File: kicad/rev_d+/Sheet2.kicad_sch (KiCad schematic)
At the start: 227 parts, among them J10 vg_old, J12 JUMPER, J13 JUMPER, J14 JUMPER, J5 JUMPER, J6 JUMPER, J8 JUMPER, J9 JUMPER, Q2 QUARTZ, Q3 QUARTZ32768, X11 KEYB-MOUSE, X12 IDC20, X13 USB_C, X15 PLB2-2, X19 WCH LinkE pgm conn, X21 Turbosound conn, X22 PS2 extra input, X23 SEGA pads, X25 USB_C device, X27 USB_A, X28 RJ45_Hanrun_HR911105A_Horizon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, X29 RS232_9, X3 IDC26LPT, X4 IDC10M, X5 IDC10M, X6 IDC10M

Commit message: pentevo: rev D+: change level shifter for PS/2 to NMOS-based (save 4 pins), connect forgotten nCONFIG/nSTATUS/CONFDONE pins
git-svn-id: svn://localhost/local-pentevo@1313 c6c76956-fad2-4150-a3a9-ea0a427205ba
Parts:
- removed C55, C62: 0.1uF, C-CHIP, symbol eva-altium-import:Sheet2_3_mirrored_CAPCHIP
- removed D15, D22: 74HCT125, symbol 74xx:74LS125
- removed R123, R124, R125, R126: 10K, R-CHIP, symbol eva-altium-import:Sheet2_3_mirrored_RESCHIP
- removed R176, R201, R202, R31: 5K1, R-CHIP, symbol eva-altium-import:Sheet2_0_RESCHIP
- added DA16, DA17, DA18: USBLC6-4SC6, Package_TO_SOT_SMD:SOT-23-6, symbol Power_Protection:USBLC6-4SC6
- added R123, R124, R125, R126, R176, R201, R202, R31: 10K, R-CHIP, symbol eva-altium-import:Sheet2_1_RESCHIP
- added VT14, VT15, VT16, VT17: 2N7002, Package_TO_SOT_SMD:SOT-23, symbol Transistor_FET:2N7002
- C56: value 20pF -> 100pF
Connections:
- net PS2_KB_CLK_O is gone; now on net ~{STATUS}: D4.18 (PC3)
- net PS2_KB_DAT_O is gone; now on net ~{CONFIG}: D4.17 (PC2)
- net PS2_MS_DAT_O is gone; now on net CONFDONE: D4.33 (PC4)
- net GND: now also DA16.2 (GND), DA17.5 (VBUS), DA18.5 (VBUS)
- net PS2_KEYB_CLK: now also DA16.3 (I/O2), R124.1 (i/o), VT15.3 (D)
- net PS2_KEYB_DAT: now also DA16.1 (I/O1), R125.1 (i/o), VT14.3 (D)
- net PS2_MOUS_CLK: now also DA16.6 (I/O4), R123.2 (i/o1), VT17.3 (D)
- net PS2_MOUS_DAT: now also DA16.4 (I/O3), R31.2 (i/o1), VT16.3 (D)
- net USBDEV+: now also DA17.1 (I/O1), DA17.6 (I/O4)
- net USBDEV-: now also DA17.3 (I/O2), DA17.4 (I/O3)
- net USBHOST+: now also DA18.1 (I/O1), DA18.6 (I/O4)
- net USBHOST-: now also DA18.3 (I/O2), DA18.4 (I/O3)
- net VCC33_MCU: now also R126.2 (i/o1), R176.2 (i/o1), R201.2 (i/o1), R202.2 (i/o1), VT14.1 (G), VT15.1 (G), VT16.1 (G), VT17.1 (G)
- net VCC5: now also DA16.5 (VBUS), R123.1 (i/o), R124.2 (i/o1), R125.2 (i/o1), R31.1 (i/o)
- net VCC5_MCU: now also DA18.2 (GND)
- net at R200.1 (i/o), X25.A4 (VBUS), X25.A9 (VBUS)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: now also DA17.2 (GND)
- net PS2_KB_CLK_I renamed PS2_KB_CLK_3v3
- net PS2_KB_CLK_3v3: now also R202.1 (i/o), VT15.2 (S)
- net PS2_KB_DAT_I renamed PS2_KB_DAT_3v3
- net PS2_KB_DAT_3v3: now also R201.1 (i/o), VT14.2 (S)
- net PS2_MS_CLK_I renamed PS2_MS_CLK_3v3
- net PS2_MS_CLK_3v3: now also R176.1 (i/o), VT17.2 (S)
- net PS2_MS_CLK_O: no longer names the net of D4.34 (PC5)
- net PS2_MS_DAT_I renamed PS2_MS_DAT_3v3
- net PS2_MS_DAT_3v3: now also R126.1 (i/o), VT16.2 (S)
- no-connect marks 37 -> 38
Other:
- moved on the sheet: C105, C122, C36, C37, C50, C56, C83, D20A, D20B, D20C, D20D, D20E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

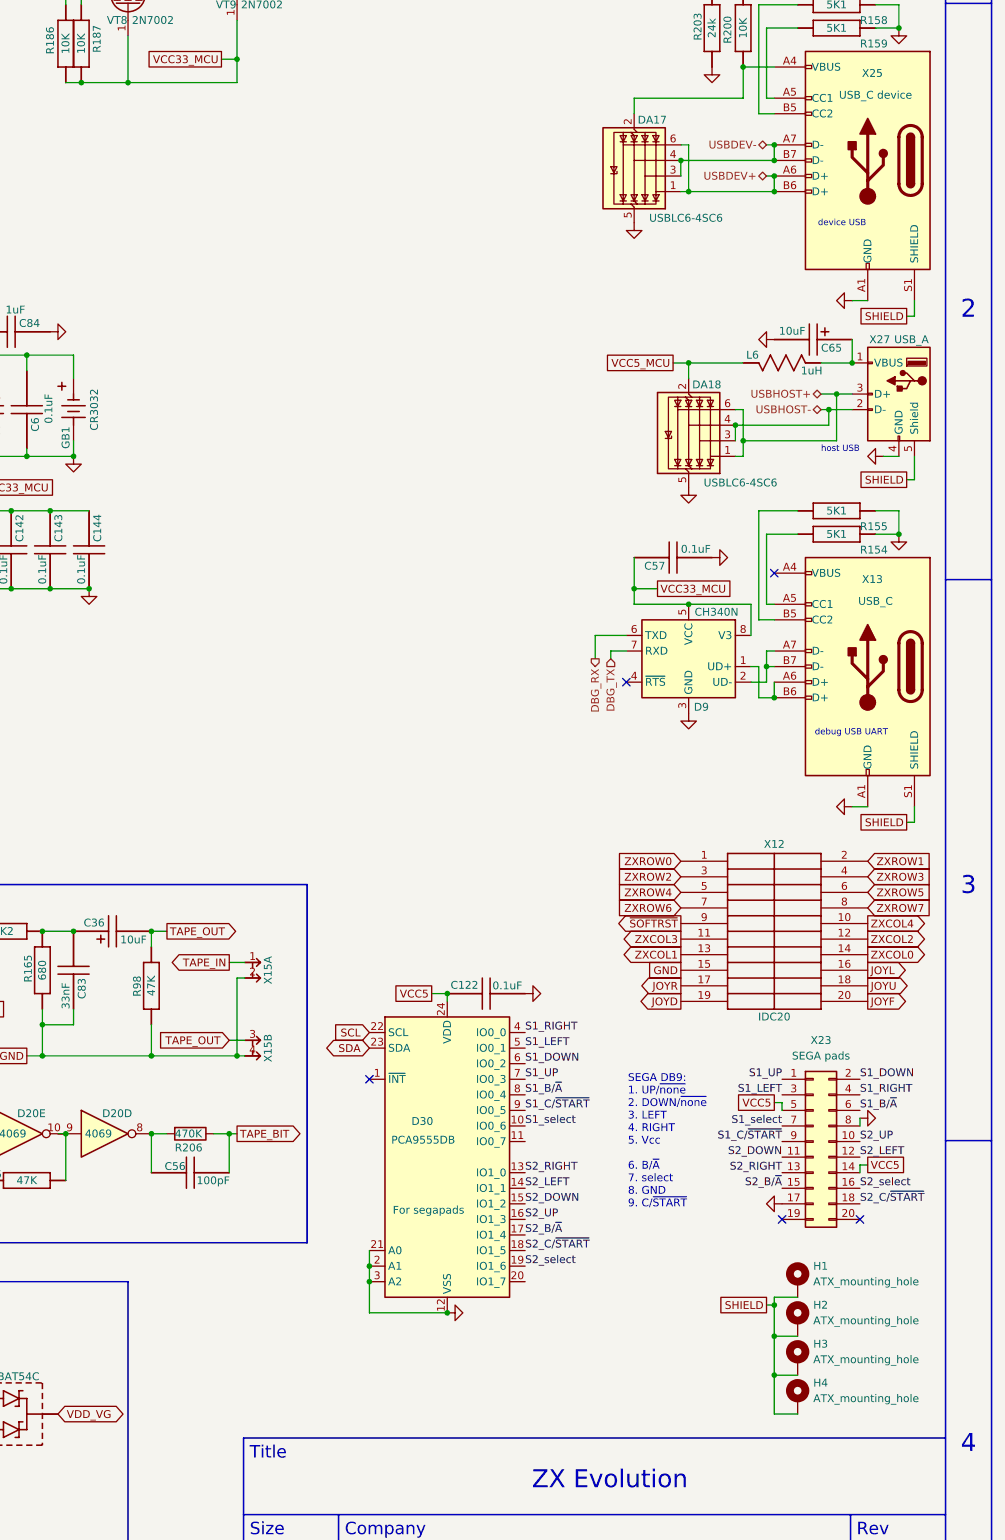
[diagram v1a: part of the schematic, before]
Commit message: pentevo: rev D+: fix USBLC6 wiring, add FE1.1s hub (WIP)
git-svn-id: svn://localhost/local-pentevo@1331 c6c76956-fad2-4150-a3a9-ea0a427205ba
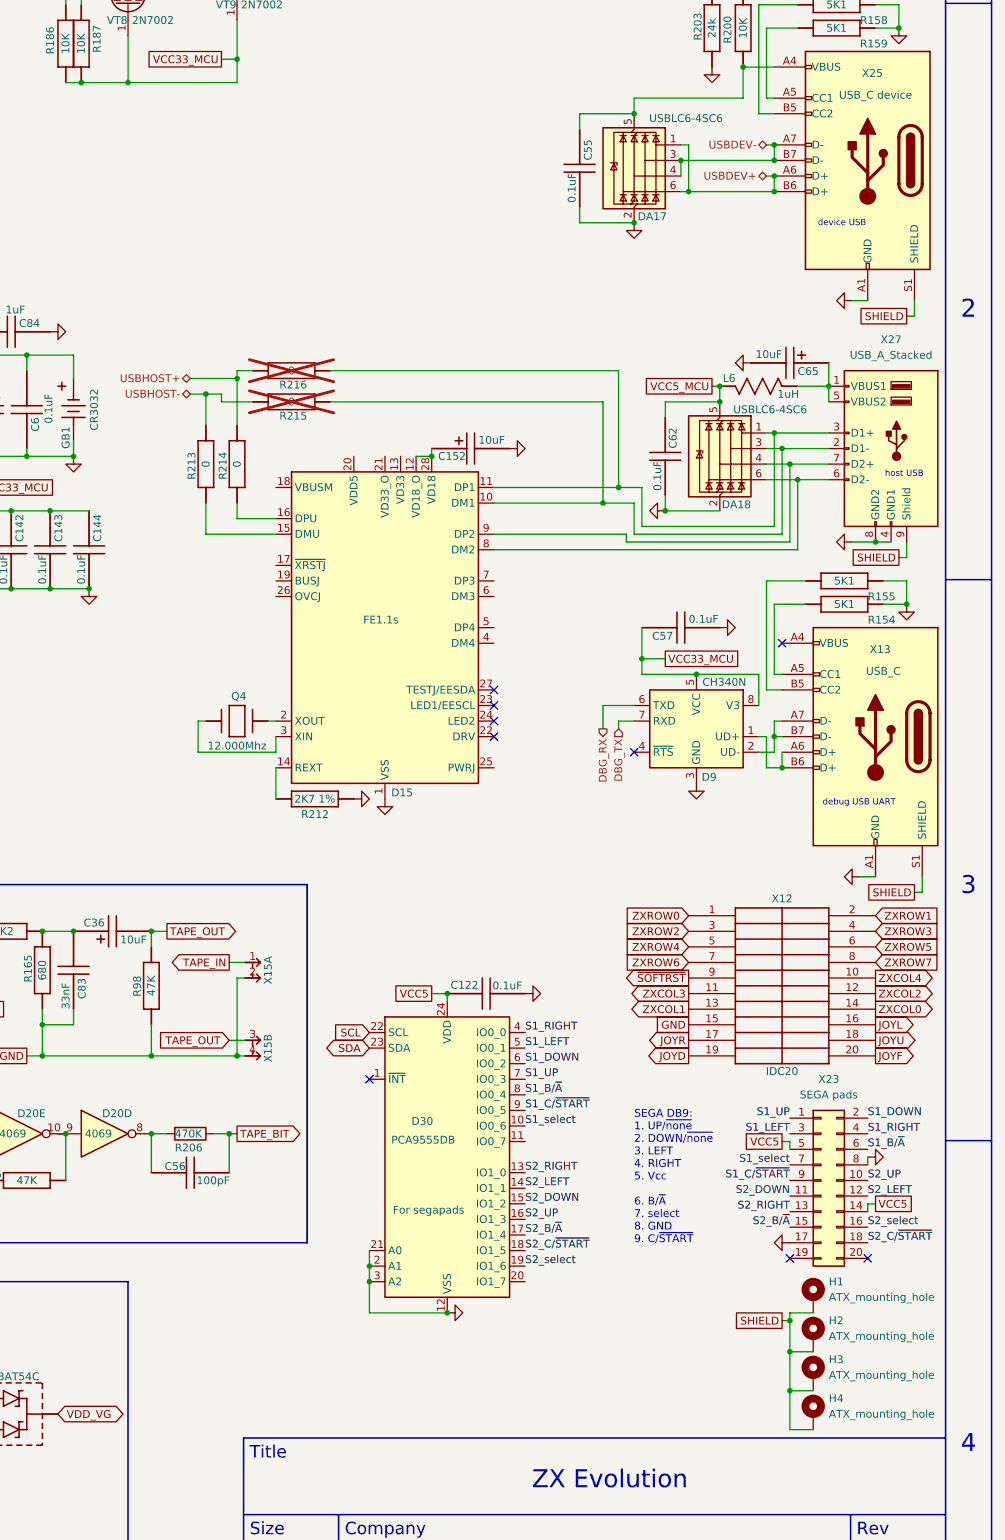
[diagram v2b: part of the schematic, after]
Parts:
- removed X27: USB_A, symbol Connector:USB_A
- added C152: 10uF, EC-CHIP, symbol eva-altium-import:Sheet2_3_ECAPCHIP
- added C55, C62: 0.1uF, C-CHIP, symbol eva-altium-import:Sheet2_2_CAPCHIP
- added D15: FE1.1s, Package_SO:SSOP-28_3.9x9.9mm_P0.635mm, symbol Interface_USB:FE1.1s
- added Q4: QUARTZ, CRYSTAL, symbol eva-altium-import:Sheet2_0_QUARTZ
- added R212: 2K7 1%, R-CHIP, symbol eva-altium-import:Sheet2_0_RESCHIP
- added R213, R214, R215, R216: 0, R-CHIP, symbol eva-altium-import:Sheet1_1_RESCHIP
- added X27: USB_A_Stacked, symbol Connector:USB_A_Stacked
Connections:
- net GND: now also DA17.2 (GND), DA18.2 (GND), C152.2, C55.2, C62.2, D15.1 (VSS), R212.1 (i/o), X27.4 (GND1), X27.8 (GND2); no longer DA17.5 (VBUS), DA18.5 (VBUS)
- net SHIELD: now also X27.9 (Shield)
- net USBHOST+: now also R214.2 (i/o1), R216.2 (i/o1); no longer DA18.1 (I/O1), DA18.6 (I/O4)
- net USBHOST-: now also R213.2 (i/o1), R215.2 (i/o1); no longer DA18.3 (I/O2), DA18.4 (I/O3)
- net VCC5_MCU: now also DA18.5 (VBUS), C62.1; no longer DA18.2 (GND)
- net at R200.1 (i/o), X25.A4 (VBUS), X25.A9 (VBUS)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: now also DA17.5 (VBUS), C55.1; no longer DA17.2 (GND)
- net at C65.1, L6.2: now also X27.1 (VBUS1), X27.5 (VBUS2)
- new net: D15.10 (DM1), DA18.3 (I/O2), R215.1 (i/o), X27.2 (D1-)
- new net: D15.11 (DP1), DA18.1 (I/O1), R216.1 (i/o), X27.3 (D1+)
- new net: D15.8 (DM2), DA18.6 (I/O4), X27.6 (D2-)
- new net: D15.9 (DP2), DA18.4 (I/O3), X27.7 (D2+)
- new net: D15.16 (DPU), R214.1 (i/o)
- new net: D15.14 (REXT), R212.2 (i/o1)
- new net: D15.3 (XIN), Q4.A
- new net: D15.2 (XOUT), Q4.B
- new net: C152.1, D15.12 (VD18_O), D15.28 (VD18)
- new net: D15.15 (DMU), R213.1 (i/o)
- no-connect marks 38 -> 42
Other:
- moved on the sheet: C57, C65, D9, H1, H2, H3, H4, L6, R154, R155, X12, X13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

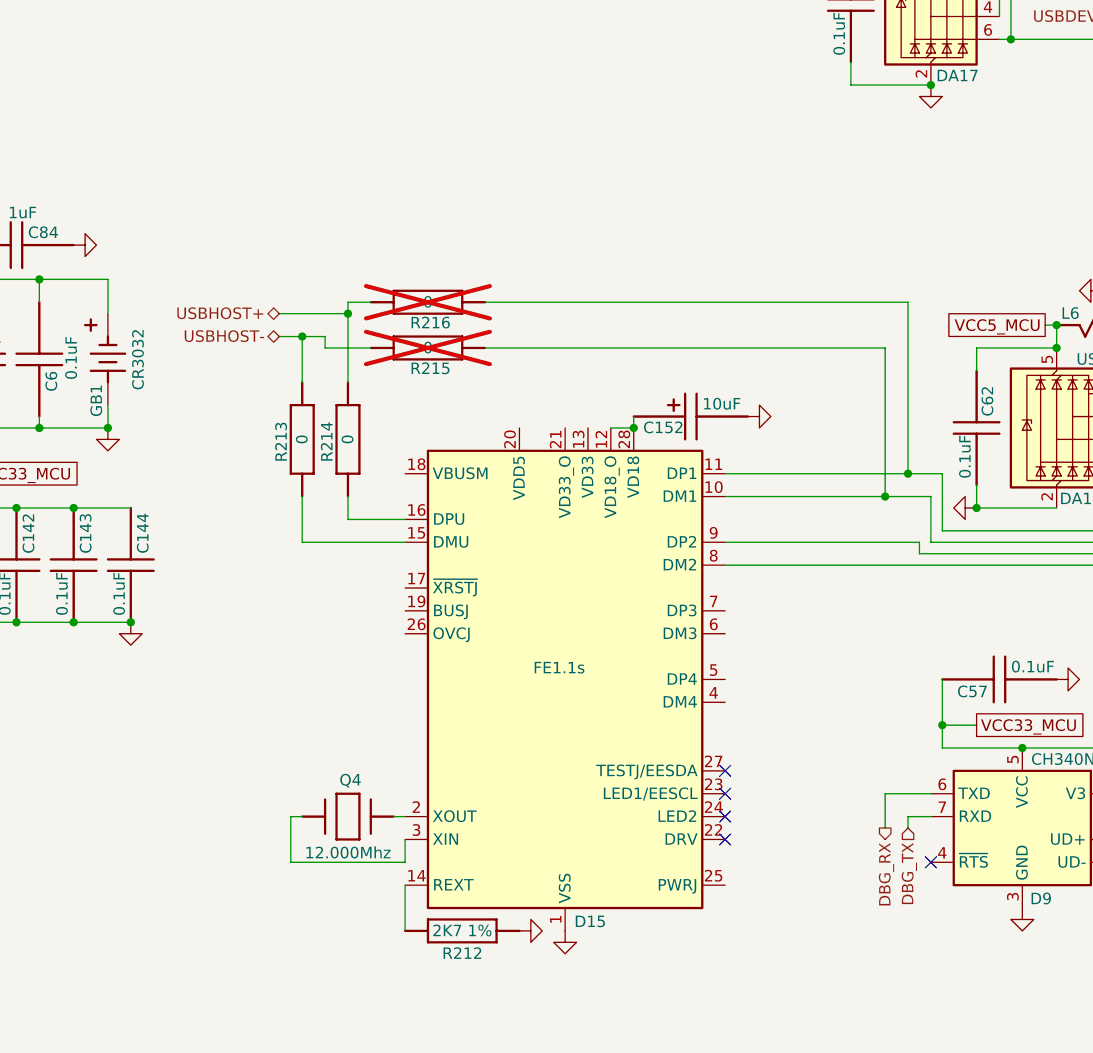
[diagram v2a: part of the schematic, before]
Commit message: pentevo: rev D+: finish FE1.1s part
git-svn-id: svn://localhost/local-pentevo@1338 c6c76956-fad2-4150-a3a9-ea0a427205ba
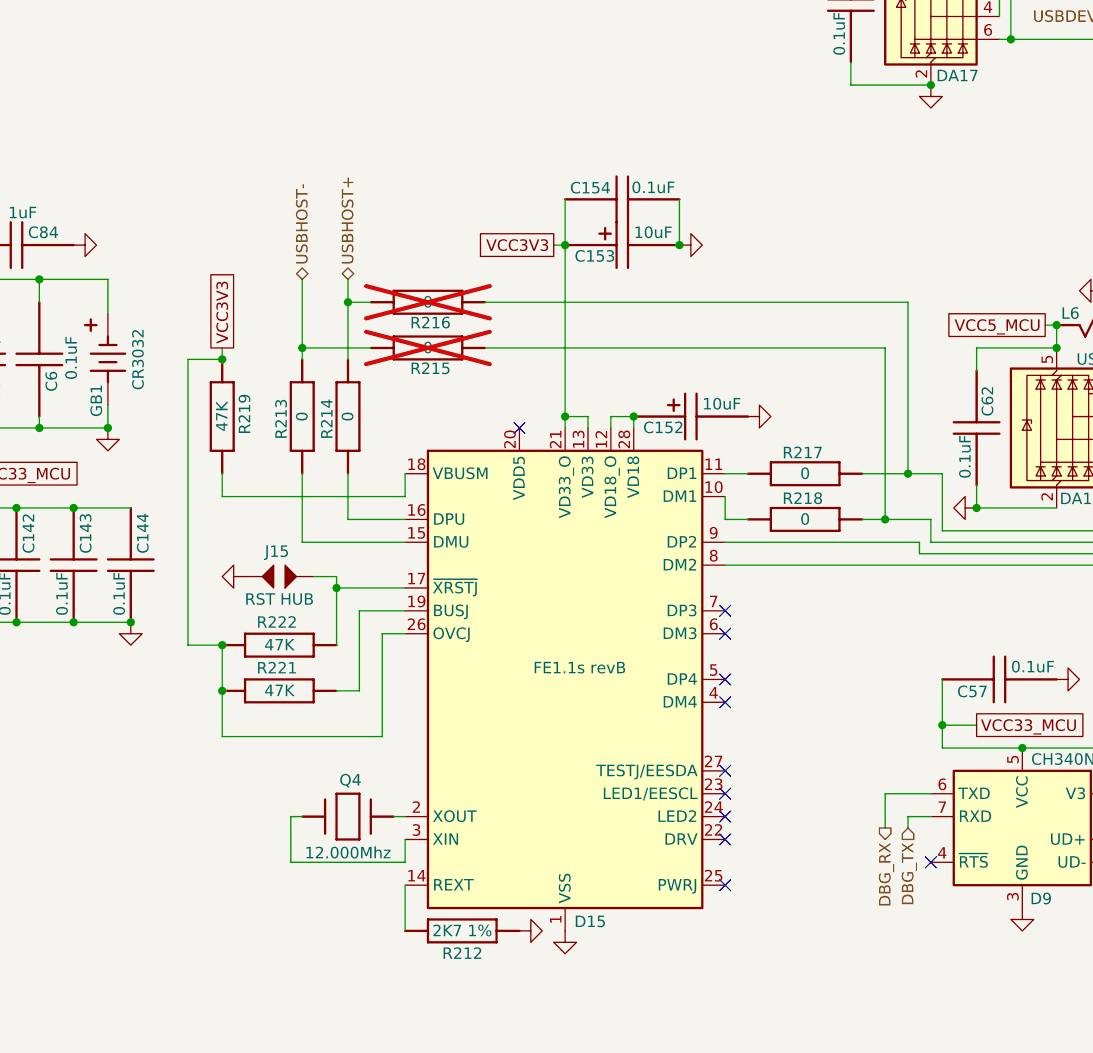
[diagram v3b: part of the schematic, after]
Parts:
- added C153: 10uF, EC-CHIP, symbol eva-altium-import:Sheet2_3_ECAPCHIP
- added C154: 0.1uF, C-CHIP, symbol eva-altium-import:Sheet2_2_CAPCHIP
- added J15: JUMPER, JUMPER, symbol eva-altium-import:Sheet2_3_JUMPER
- added R217, R218: 0, R-CHIP, symbol eva-altium-import:Sheet1_1_RESCHIP
- added R219, R221, R222: 47K, R-CHIP, symbol eva-altium-import:Sheet2_0_RESCHIP
- D15: value FE1.1s -> FE1.1s revB
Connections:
- net GND: now also C153.2, C154.2, J15.1 (2)
- net VCC3V3: now also D15.13 (VD33), D15.21 (VD33_O), D15.26 (OVCJ), C153.1, C154.1, R219.1 (i/o), R221.1 (i/o), R222.1 (i/o)
- net at DA18.3 (I/O2), R215.1 (i/o), X27.2 (D1-): now also R218.2 (i/o1); no longer D15.10 (DM1)
- net at DA18.1 (I/O1), R216.1 (i/o), X27.3 (D1+): now also R217.2 (i/o1); no longer D15.11 (DP1)
- net at D15.17 (~{XRSTJ}): now also J15.0 (1), R222.2 (i/o1)
- net at D15.18 (VBUSM): now also R219.2 (i/o1)
- net at D15.19 (BUSJ): now also R221.2 (i/o1)
- new net: D15.11 (DP1), R217.1 (i/o)
- new net: D15.10 (DM1), R218.1 (i/o)
- no-connect marks 42 -> 48
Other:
- moved on the sheet: R213, R214

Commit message: pentevo: rev D+: add options for OPAMPs, replace 2N7002 with BSS138
git-svn-id: svn://localhost/local-pentevo@1342 c6c76956-fad2-4150-a3a9-ea0a427205ba
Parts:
- removed VT14, VT15, VT16, VT17, VT8, VT9: 2N7002, Package_TO_SOT_SMD:SOT-23, symbol Transistor_FET:2N7002
- added VT14, VT15, VT16, VT17, VT8, VT9: BSS138, Package_TO_SOT_SMD:SOT-23, symbol Transistor_FET:BSS138
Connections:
- net PS2_KB_CLK_3v3: now also VT15.2 (S)
- net PS2_KB_DAT_3v3: now also VT14.2 (S)
- net PS2_KEYB_CLK: now also VT15.3 (D)
- net PS2_KEYB_DAT: now also VT14.3 (D)
- net PS2_MOUS_CLK: now also VT17.3 (D)
- net PS2_MOUS_DAT: now also VT16.3 (D)
- net PS2_MS_CLK_3v3: now also VT17.2 (S)
- net PS2_MS_DAT_3v3: now also VT16.2 (S)
- net SCL: now also VT9.3 (D)
- net SCL_33: now also VT9.2 (S)
- net SDA: now also VT8.3 (D)
- net SDA_33: now also VT8.2 (S)
- net VCC33_MCU: now also VT14.1 (G), VT15.1 (G), VT16.1 (G), VT17.1 (G), VT8.1 (G), VT9.1 (G)

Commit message: pentevo: rev D+: add more usblc6, rearrange a bit
git-svn-id: svn://localhost/local-pentevo@1347 c6c76956-fad2-4150-a3a9-ea0a427205ba
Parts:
- added VD10, VD23, VD24, VD25, VD26, VD27, VD28, VD5, VD9: USBLC6-4SC6, Package_TO_SOT_SMD:SOT-23-6, symbol Power_Protection:USBLC6-4SC6
- added VT6, VT7: BC857, Package_TO_SOT_SMD:SOT-23_Handsoldering, symbol Transistor_BJT:BC857
- renumbered DA17 to VD20, DA18 to VD21, DA16 to VD22
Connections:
- net GND: now also X23.19 (Pin_19), VD10.2 (GND), VD23.2 (GND), VD24.2 (GND), VD25.2 (GND), VD26.2 (GND), VD27.2 (GND), VD28.2 (GND), VD5.2 (GND), VD9.2 (GND), VT6.3 (C), VT7.3 (C); no longer X23.17 (Pin_17)
- net JOYD: now also VD24.1 (I/O1)
- net JOYF: now also VD24.6 (I/O4)
- net JOYL: now also VD24.3 (I/O2)
- net JOYR: now also VD24.4 (I/O3)
- net JOYU: now also VD25.6 (I/O4)
- net NMIKEY: now also VD28.3 (I/O2)
- net S1_B/~{A}: now also VD10.1 (I/O1)
- net S1_C/~{START}: now also VD10.3 (I/O2)
- net S1_DOWN: now also VD5.4 (I/O3)
- net S1_LEFT: now also VD5.3 (I/O2)
- net S1_RIGHT: now also VD5.1 (I/O1)
- net S1_UP: now also VD5.6 (I/O4)
- net S1_select: now also VD10.4 (I/O3)
- net S2_B/~{A}: now also X23.17 (Pin_17), VD9.6 (I/O4); no longer X23.15 (Pin_15)
- net S2_C/~{START}: now also X23.20 (Pin_20), VD23.4 (I/O3); no longer X23.18 (Pin_18)
- net S2_DOWN: now also X23.13 (Pin_13), VD9.3 (I/O2); no longer X23.11 (Pin_11)
- net S2_LEFT: now also X23.14 (Pin_14), VD9.1 (I/O1); no longer X23.12 (Pin_12)
- net S2_RIGHT: now also X23.15 (Pin_15), VD10.6 (I/O4); no longer X23.13 (Pin_13)
- net S2_UP: now also X23.12 (Pin_12), VD9.4 (I/O3); no longer X23.10 (Pin_10)
- net S2_select: now also X23.18 (Pin_18), VD23.6 (I/O4); no longer X23.16 (Pin_16)
- net VCC33_MCU: now also VD24.5 (VBUS), VD25.5 (VBUS), VD26.5 (VBUS), VD27.5 (VBUS), VD28.5 (VBUS)
- net VCC5: now also X23.16 (Pin_16), VD10.5 (VBUS), VD23.5 (VBUS), VD5.5 (VBUS), VD9.5 (VBUS); no longer X23.14 (Pin_14)
- net ZXCOL0: now also VD27.4 (I/O3)
- net ZXCOL1: now also VD27.3 (I/O2)
- net ZXCOL2: now also VD27.1 (I/O1)
- net ZXCOL3: now also VD28.1 (I/O1)
- net ZXCOL4: now also VD28.6 (I/O4)
- net ZXROW0: now also VD25.4 (I/O3)
- net ZXROW1: now also VD25.3 (I/O2)
- net ZXROW2: now also VD25.1 (I/O1)
- net ZXROW3: now also VD26.1 (I/O1)
- net ZXROW4: now also VD26.3 (I/O2)
- net ZXROW5: now also VD26.4 (I/O3)
- net ZXROW6: now also VD26.6 (I/O4)
- net ZXROW7: now also VD27.6 (I/O4)
- net ~{SOFTRST}: now also VD28.4 (I/O3)
- net ~{DISK_LED}: no longer names the net of R19.2 (i/o1), R205.2 (i/o1), VT12.3 (C)
- net ~{DISK_LED}: now also VT6.2 (E), VT7.2 (E)
- new net ~{DASP}: VT6.1 (B)
- new net ~{SDCS}: VT7.1 (B)
- no-connect marks 48 -> 46
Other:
- note added: "LED control"
- note added: "MCU power"
- note added: "SEGA pads"
- moved on the sheet: C105, C145, C148, C149, C150, C151, C36, C37, C56, C83, D13D, D20A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
